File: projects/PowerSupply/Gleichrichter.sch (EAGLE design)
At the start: 11 parts

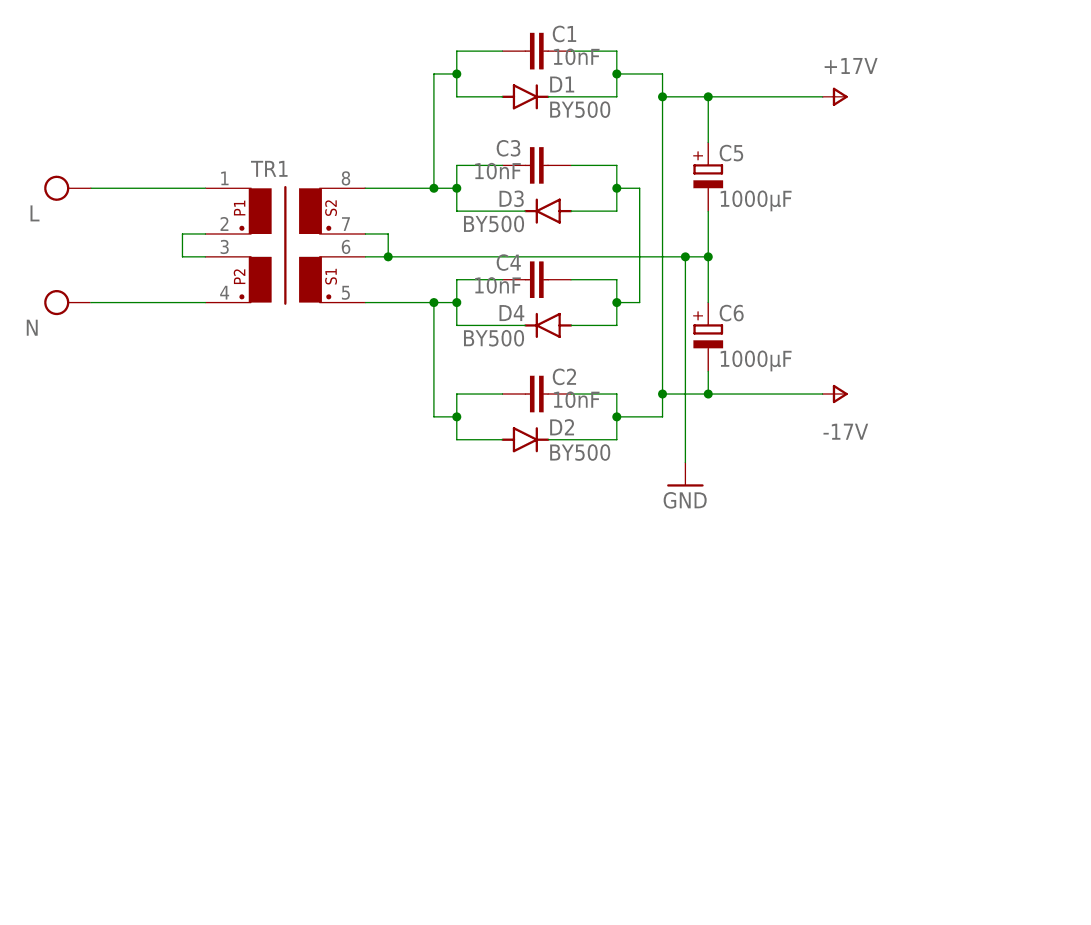
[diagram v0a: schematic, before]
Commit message: feat: power supply
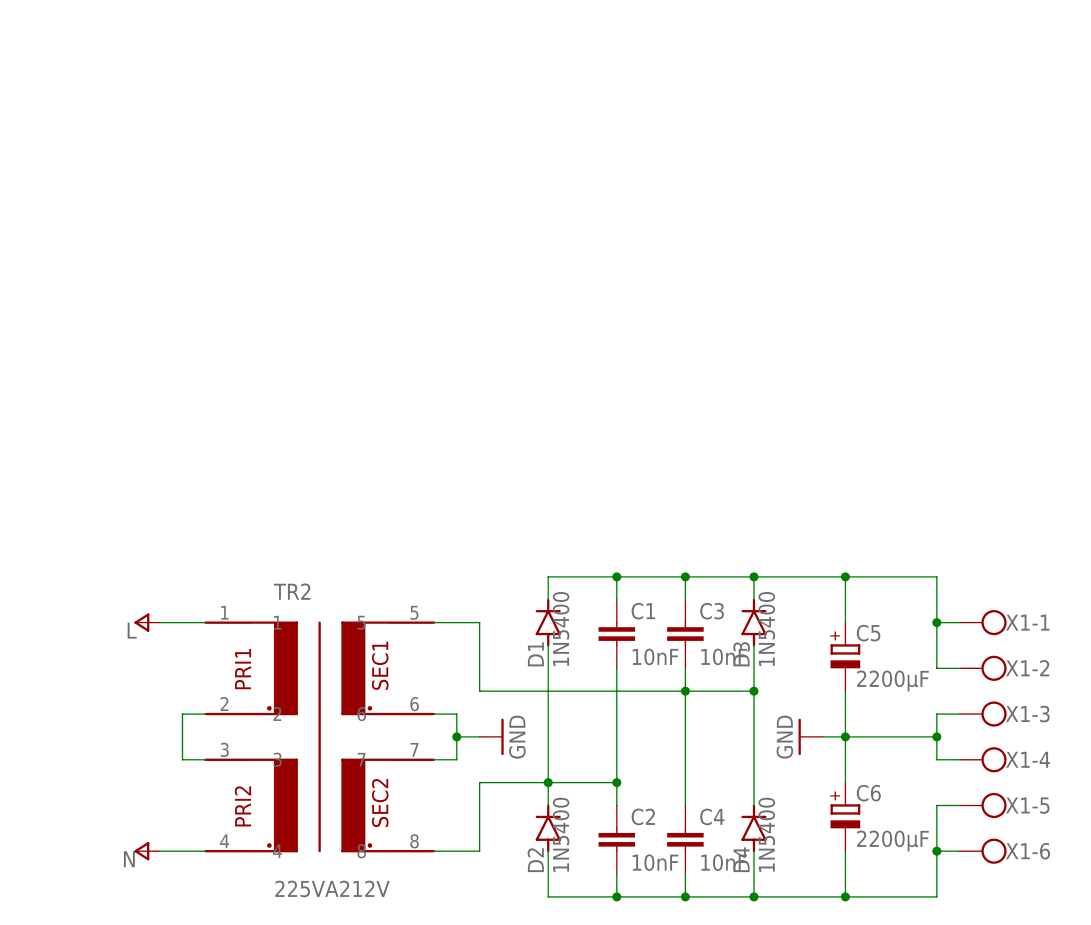
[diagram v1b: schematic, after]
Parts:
- removed TR1: (no value), trafo:FL52
- added TR2, U$1, U$2, U$3, U$4, U$5, U$6: 225VA212V, bb84:225VA212V
- added X1: (no value), con-wago-500:W237-6
- C5, C6: value 1000µF -> 2200µF; device rcl:CPOL-EUE5-10.5 -> rcl:CPOL-EUE5-13
- D1, D2, D3, D4: value BY500 -> 1N5400; device diode:BY500 -> diode:1N5400
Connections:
- removed net N$6: C2.2, C4.1, D2.A, D4.C, TR1.5
- removed net V-: C1.1, C2.1, C5.+, C6.-, D1.C, D2.C
- removed net VCC: TR1.1, TR1.4
- new net N$3: TR2.2, TR2.3
- new net N$4: C1.2, C2.1, D1.A, D2.C, TR2.8
- new net V+: TR2.1, TR2.4
- net GND: now also TR2.6, TR2.7, X1-3.KL, X1-4.KL; no longer TR1.6, TR1.7
- net N$1: now also C3.2, C4.1, D3.A, D4.C, TR2.5; no longer TR1.2, TR1.3
- net N$2: now also C2.2, C4.2, C6.-, D2.A, D4.A, X1-5.KL, X1-6.KL; no longer C1.2, C3.1, D1.A, D3.C, TR1.8
- net N$5: now also C1.1, C3.1, C5.+, D1.C, D3.C, X1-1.KL, X1-2.KL; no longer C3.2, C4.2, D3.A, D4.A
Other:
- moved on the sheet: C1, C2, C3, C4, C5, C6, D1, D2, D3, D4

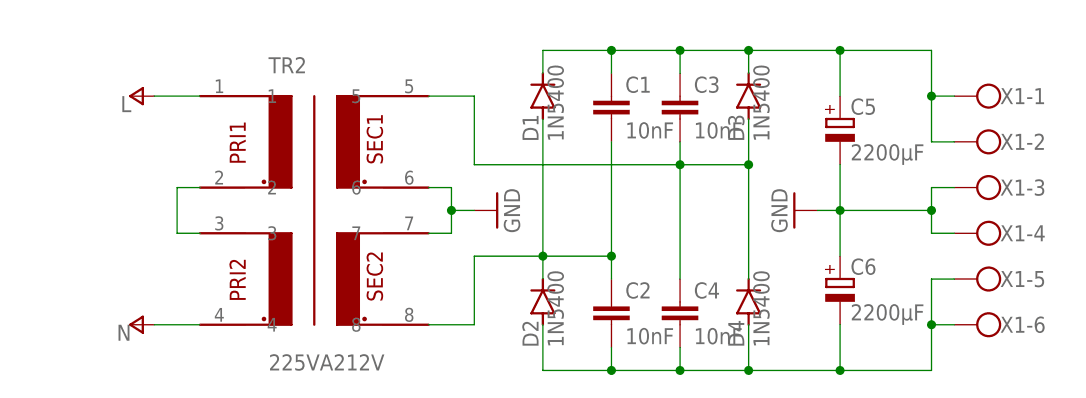
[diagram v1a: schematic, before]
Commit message: feat: power supply
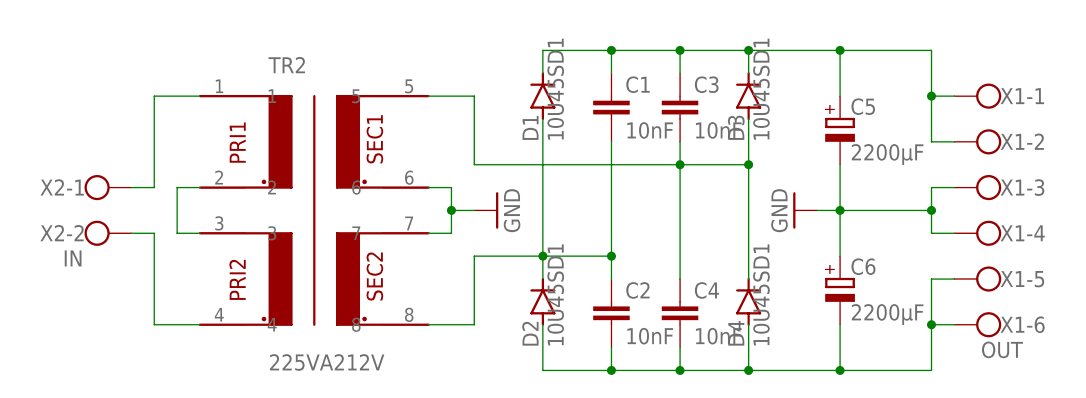
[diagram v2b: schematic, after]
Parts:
- removed U$1, U$2, U$3, U$4, U$5, U$6: 225VA212V, bb84:225VA212V
- added X2: IN, con-wago-500:W237-102
- D1, D2, D3, D4: value 1N5400 -> 10U45SD1
- X1: value (none) -> OUT
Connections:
- removed net V+: TR2.1, TR2.4
- new net N$6: TR2.4, X2-2.KL
- new net N$7: TR2.1, X2-1.KL
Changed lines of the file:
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@@
 </classes>
 <parts>
-<part name="U$1" library="bb84" deviceset="225VA212V" device=""/>
-<part name="U$2" library="bb84" deviceset="225VA212V" device=""/>
-<part name="U$3" library="bb84" deviceset="225VA212V" device=""/>
-<part name="U$4" library="bb84" deviceset="225VA212V" device=""/>
-<part name="U$5" library="bb84" deviceset="225VA212V" device=""/>
-<part name="U$6" library="bb84" deviceset="225VA212V" device=""/>
 <part name="TR2" library="bb84" deviceset="225VA212V" device=""/>
 <part name="GND2" library="supply1" library_urn="urn:adsk.eagle:library:371" deviceset="GND" device=""/>
-<part name="D1" library="diode" library_urn="urn:adsk.eagle:library:210" deviceset="1N5400" device="" package3d_urn="urn:adsk.eagle:package:43365/2"/>
-<part name="D2" library="diode" library_urn="urn:adsk.eagle:library:210" deviceset="1N5400" device="" package3d_urn="urn:adsk.eagle:package:43365/2"/>
-<part name="D3" library="diode" library_urn="urn:adsk.eagle:library:210" deviceset="1N5400" device="" package3d_urn="urn:adsk.eagle:package:43365/2"/>
-<part name="D4" library="diode" library_urn="urn:adsk.eagle:library:210" deviceset="1N5400" device="" package3d_urn="urn:adsk.eagle:package:43365/2"/>
+<part name="D1" library="diode" library_urn="urn:adsk.eagle:library:210" deviceset="1N5400" device="" package3d_urn="urn:adsk.eagle:package:43365/2" value="10U45SD1"/>
+<part name="D2" library="diode" library_urn="urn:adsk.eagle:library:210" deviceset="1N5400" device="" package3d_urn="urn:adsk.eagle:package:43365/2" value="10U45SD1"/>
+<part name="D3" library="diode" library_urn="urn:adsk.eagle:library:210" deviceset="1N5400" device="" package3d_urn="urn:adsk.eagle:package:43365/2" value="10U45SD1"/>
+<part name="D4" library="diode" library_urn="urn:adsk.eagle:library:210" deviceset="1N5400" device="" package3d_urn="urn:adsk.eagle:package:43365/2" value="10U45SD1"/>
 <part name="C1" library="rcl" library_urn="urn:adsk.eagle:library:334" deviceset="C-EU" device="050-024X044" package3d_urn="urn:adsk.eagle:package:23643/1" value="10nF"/>
 <part name="C2" library="rcl" library_urn="urn:adsk.eagle:library:334" deviceset="C-EU" device="050-024X044" package3d_urn="urn:adsk.eagle:package:23643/1" value="10nF"/>
@@
 <part name="C5" library="rcl" library_urn="urn:adsk.eagle:library:334" deviceset="CPOL-EU" device="E5-13" package3d_urn="urn:adsk.eagle:package:23375/1" value="2200µF"/>
 <part name="C6" library="rcl" library_urn="urn:adsk.eagle:library:334" deviceset="CPOL-EU" device="E5-13" package3d_urn="urn:adsk.eagle:package:23375/1" value="2200µF"/>
-<part name="X1" library="con-wago-500" library_urn="urn:adsk.eagle:library:195" deviceset="W237-6" device="" package3d_urn="urn:adsk.eagle:package:10696/1"/>
-<part name="P+1" library="supply1" library_urn="urn:adsk.eagle:library:371" deviceset="V+" device="" value="L"/>
-<part name="P+2" library="supply1" library_urn="urn:adsk.eagle:library:371" deviceset="V+" device="" value="N"/>
+<part name="X1" library="con-wago-500" library_urn="urn:adsk.eagle:library:195" deviceset="W237-6" device="" package3d_urn="urn:adsk.eagle:package:10696/1" value="OUT"/>
+<part name="X2" library="con-wago-500" library_urn="urn:adsk.eagle:library:195" deviceset="W237-102" device="" package3d_urn="urn:adsk.eagle:package:10688/1" value="IN"/>
 </parts>
 <sheets>
@@
 <attribute name="NAME" x="93.98" y="-11.811" size="1.778" layer="95" rot="MR180"/>
 </instance>
-<instance part="P+1" gate="1" x="-2.54" y="12.7" smashed="yes" rot="R90">
-<attribute name="VALUE" x="-2.54" y="12.7" size="1.778" layer="96" rot="R180"/>
-</instance>
-<instance part="P+2" gate="1" x="-2.54" y="-12.7" smashed="yes" rot="R90">
-<attribute name="VALUE" x="-2.54" y="-12.7" size="1.778" layer="96" rot="R180"/>
+<instance part="X2" gate="-1" x="-7.62" y="2.54" smashed="yes">
+<attribute name="NAME" x="-7.62" y="3.429" size="1.778" layer="95" rot="R180"/>
+</instance>
+<instance part="X2" gate="-2" x="-7.62" y="-2.54" smashed="yes">
+<attribute name="VALUE" x="-10.16" y="-6.223" size="1.778" layer="96"/>
+<attribute name="NAME" x="-7.62" y="-1.651" size="1.778" layer="95" rot="R180"/>
 </instance>
 </instances>
@@
 </segment>
 </net>
-<net name="V+" class="0">
-<segment>
-<pinref part="P+1" gate="1" pin="V+"/>
+<net name="N$6" class="0">
+<segment>
+<pinref part="TR2" gate="G$1" pin="4"/>
+<wire x1="5.08" y1="-12.7" x2="0" y2="-12.7" width="0.1524" layer="91"/>
+<wire x1="0" y1="-12.7" x2="0" y2="-2.54" width="0.1524" layer="91"/>
+<pinref part="X2" gate="-2" pin="KL"/>
+<wire x1="0" y1="-2.54" x2="-2.54" y2="-2.54" width="0.1524" layer="91"/>
+</segment>
+</net>
+<net name="N$7" class="0">
+<segment>
 <pinref part="TR2" gate="G$1" pin="1"/>
-<wire x1="0" y1="12.7" x2="5.08" y2="12.7" width="0.1524" layer="91"/>
-</segment>
-<segment>
-<pinref part="TR2" gate="G$1" pin="4"/>
-<pinref part="P+2" gate="1" pin="V+"/>
-<wire x1="5.08" y1="-12.7" x2="0" y2="-12.7" width="0.1524" layer="91"/>
-</segment>
-</net>
+<wire x1="5.08" y1="12.7" x2="0" y2="12.7" width="0.1524" layer="91"/>
+<wire x1="0" y1="12.7" x2="0" y2="2.54" width="0.1524" layer="91"/>
+<pinref part="X2" gate="-1" pin="KL"/>
+<wire x1="0" y1="2.54" x2="-2.54" y2="2.54" width="0.1524" layer="91"/>
+</segment>
+</net>
